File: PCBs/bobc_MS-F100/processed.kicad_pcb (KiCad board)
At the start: 2 copper layers, 50.8 x 17.8 mm, 33 parts, among them M1 LOGO_OSHW, M2 PCB_GREEN_RMC, P1 USBCONN, P2 CONN_20, P3 CONN_20, P4 SWD, Q1 BSS84, SW1 RST, SW2 BUT, U1 MCP1703_SOT23, U2 STM32F1xx, U3 MCP1703_SOT23, U4 NUF2042, X1 8MHz

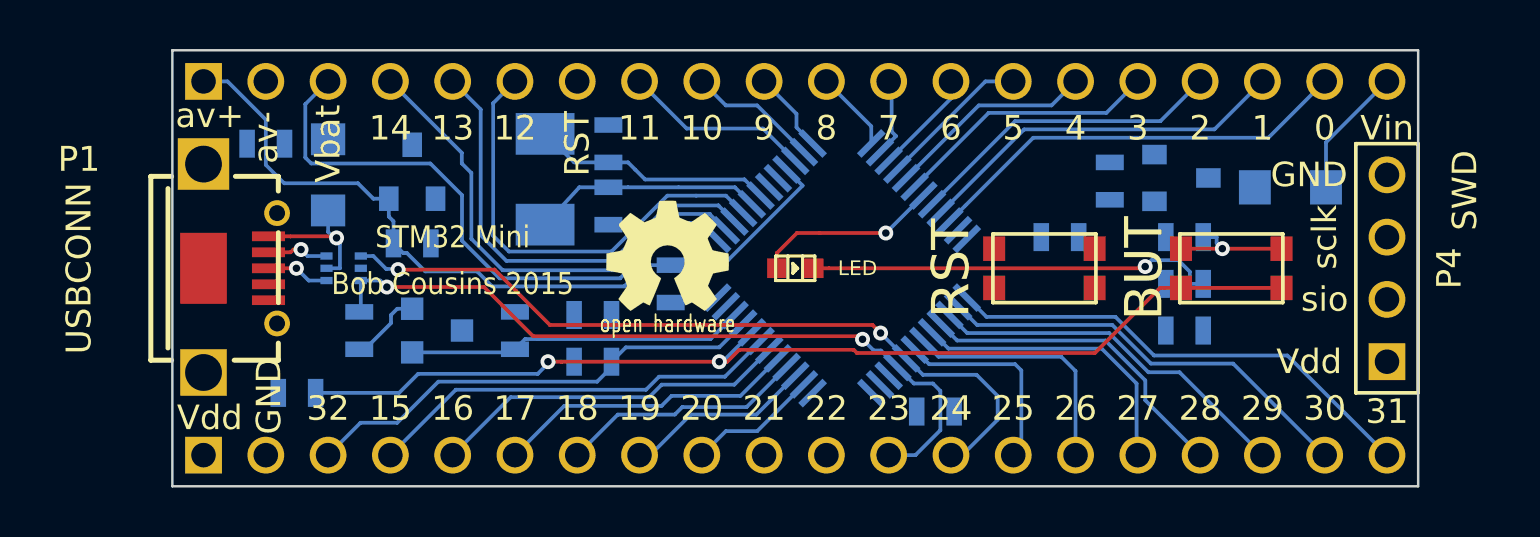
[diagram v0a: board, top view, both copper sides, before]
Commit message: recheck all circuits and clean up fill zone by rerouting the nets using freerouting and manually
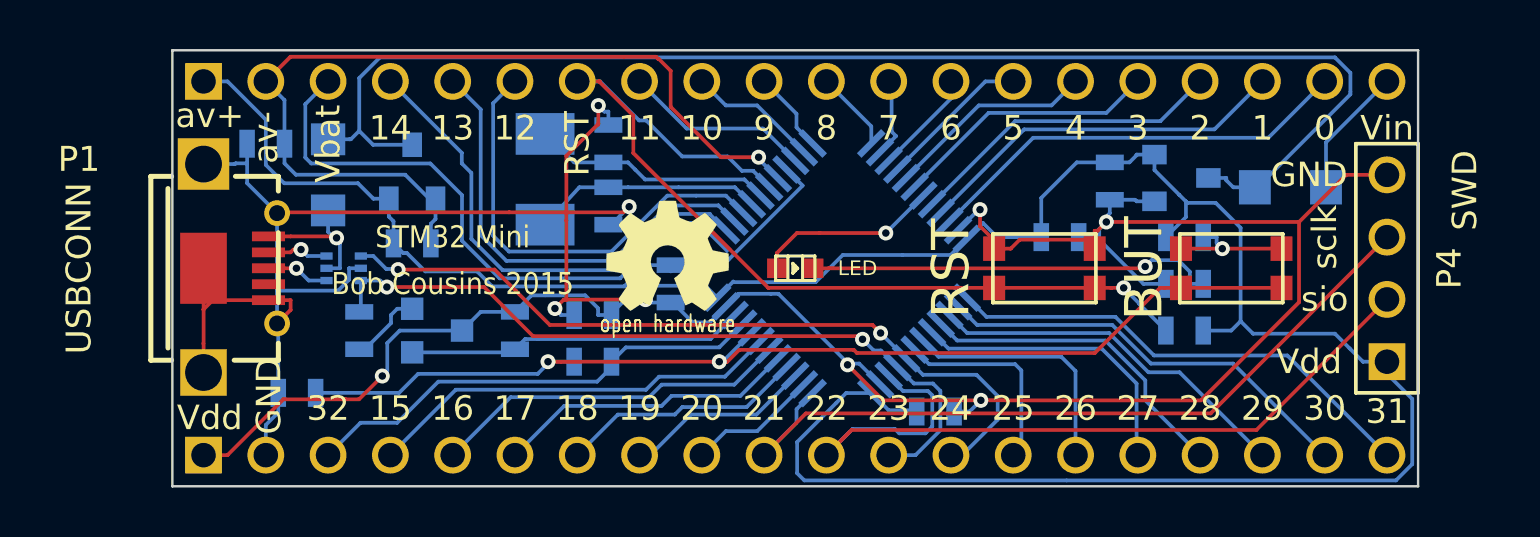
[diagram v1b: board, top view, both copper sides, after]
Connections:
- C1 pad 2: (no net) -> GND
- C2 pad 2: (no net) -> GND
- C3 pad 1: (no net) -> VDD
- C3 pad 2: (no net) -> GND
- C4 pad 2: (no net) -> /AV-
- C5 pad 1: (no net) -> VDD
- C5 pad 2: (no net) -> GND
- C6 pad 1: (no net) -> VDD
- C6 pad 2: (no net) -> GND
- C7 pad 1: (no net) -> VDD
- C7 pad 2: (no net) -> GND
- C8 pad 2: (no net) -> GND
- D2 pad 2: (no net) -> N-0000036
- D3 pad 2: (no net) -> N-0000036
- L1 pad 1: (no net) -> GND
- L1 pad 2: (no net) -> /AV-
- P1 pad 4: (no net) -> GND
- P1 pad 5: (no net) -> GND
- P2 pad 2: (no net) -> /AV-
- P2 pad 7: (no net) -> /nRESET
- P3 pad 1: (no net) -> VDD
- P3 pad 10: (no net) -> /D21_SWCLK
- P3 pad 11: (no net) -> /D22_SWIO
- P3 pad 2: (no net) -> GND
- P4 pad 1: (no net) -> VDD
- P4 pad 2: (no net) -> /D22_SWIO
- P4 pad 3: (no net) -> /D21_SWCLK
- P4 pad 4: (no net) -> GND
- Q1 pad D: (no net) -> VDD
- R1 pad 1: (no net) -> VDD
- R1 pad 2: (no net) -> /nRESET
- R2 pad 2: (no net) -> GND
- R4 pad 1: (no net) -> VDD
- R5 pad 2: (no net) -> GND
- R7 pad 1: (no net) -> VDD
- SW1 pad 1: (no net) -> GND
- SW1 pad 2: (no net) -> /nRESET
- U1 pad 1: (no net) -> GND
- U1 pad 2: (no net) -> VDD
- U1 pad 3: (no net) -> N-0000036
- U2 pad 23: (no net) -> GND
- U2 pad 24: (no net) -> VDD
- U2 pad 34: (no net) -> /D22_SWIO
- U2 pad 35: (no net) -> GND
- U2 pad 36: (no net) -> VDD
- U2 pad 37: (no net) -> /D21_SWCLK
- U2 pad 47: (no net) -> GND
- U2 pad 48: (no net) -> VDD
- U2 pad 7: (no net) -> /nRESET
- U2 pad 8: (no net) -> /AV-
- U3 pad 1: (no net) -> /AV-
- U3 pad 3: (no net) -> N-0000036
- U4 pad 2: (no net) -> GND
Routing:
- net GND: track 0.00 -> 124.8 mm, vias 0 -> 8
- net VDD: track 0.00 -> 103.9 mm, vias 0 -> 1
- net N-0000036: track 0.00 -> 55.4 mm
- net /nRESET: track 0.00 -> 38.8 mm, vias 0 -> 1
- net /AV-: track 0.00 -> 36.6 mm, vias 0 -> 1
- net /D22_SWIO: track 0.00 -> 33.8 mm
- net /D21_SWCLK: track 0.00 -> 32.4 mm
